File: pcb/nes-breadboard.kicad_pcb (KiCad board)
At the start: 2 copper layers, 44.4 x 38.1 mm, 2 parts, among them J1 Conn_01x07, J2 NES_Port_Male

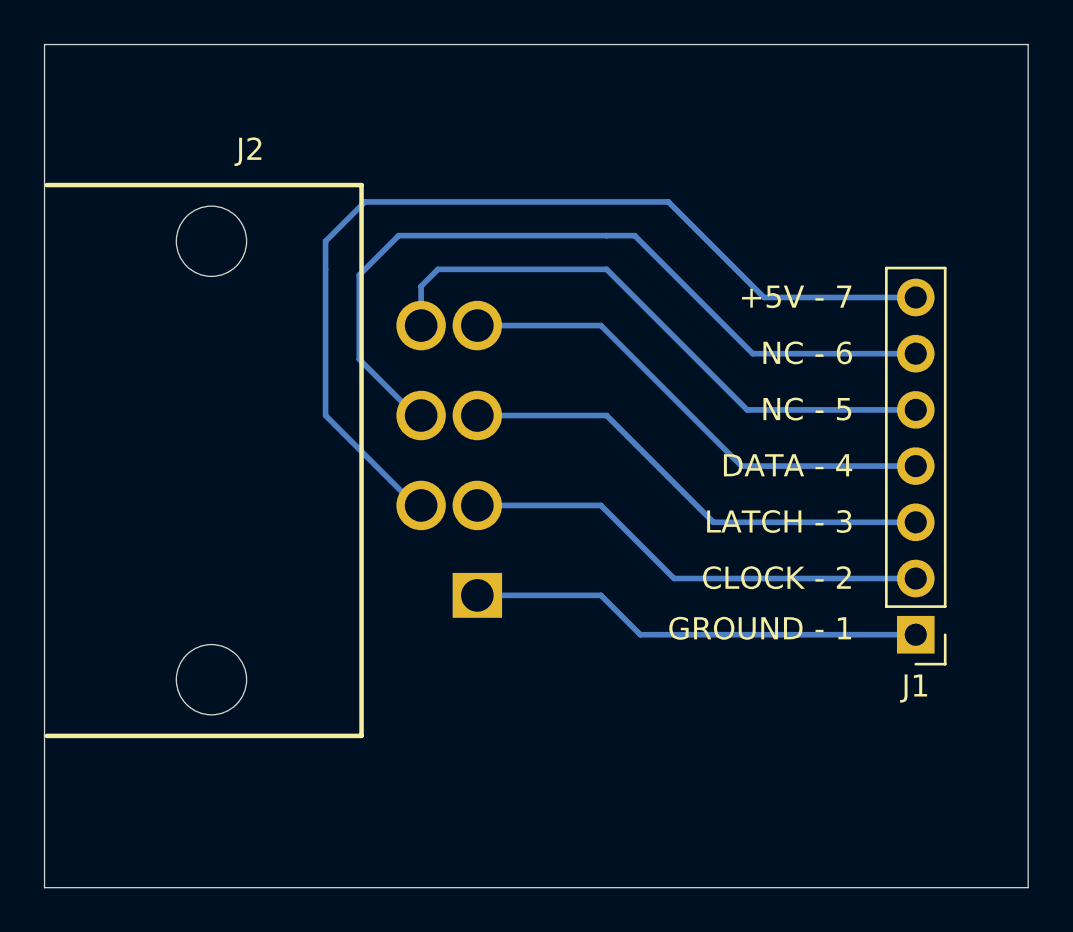
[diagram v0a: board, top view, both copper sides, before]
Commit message: Squish board to 1.5x1.5
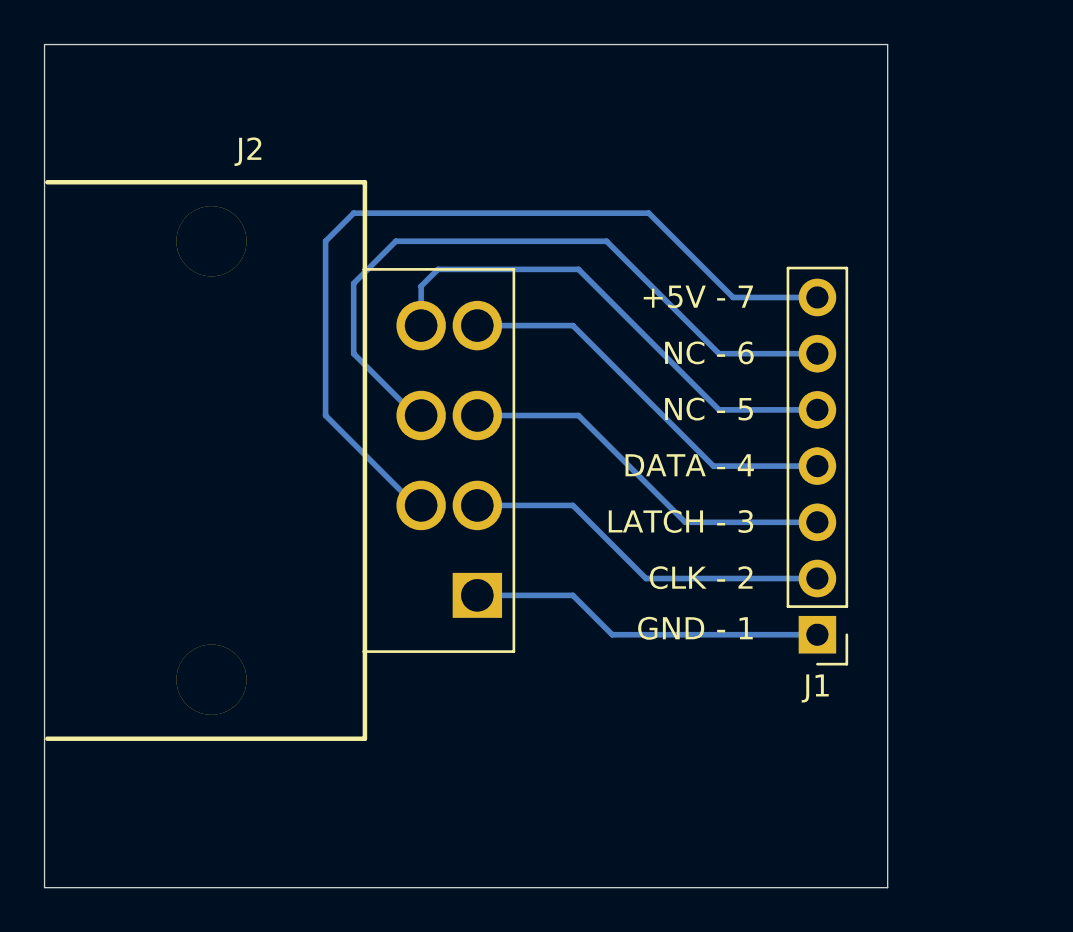
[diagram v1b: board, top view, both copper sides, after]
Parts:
- moved J1 4.44 mm to (161.9, 115.6)
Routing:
- net Net-(J1-Pad7): track 43.2 -> 38.3 mm
- net Net-(J1-Pad6): track 35.9 -> 31.3 mm
- net Net-(J1-Pad5): track 27.1 -> 22.6 mm
- net Net-(J1-Pad3): track 21.8 -> 17.4 mm
- net Net-(J1-Pad4): track 22.4 -> 18.0 mm
- net Net-(J1-Pad2): track 21.2 -> 16.7 mm
- net Net-(J1-Pad1): track 20.5 -> 16.1 mm
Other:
- board size 44.4 x 38.1 mm -> 38.1 x 38.1 mm
- board text added: "CLK - 2"
- board text added: "GND - 1"
- board text removed: "CLOCK - 2"
- board text removed: "GROUND - 1"
